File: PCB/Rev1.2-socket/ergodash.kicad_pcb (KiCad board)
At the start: 2 copper layers, 149.9 x 127.4 mm, 187 parts, among them J1 5PIN, J2 Conn_01x03, J3 Conn_01x03, J4 GS3, J5 GS3, M1 Speaker, Q1 IRLML6344TRPbF, SW1 SW_PUSH, SW10 SW_PUSH, SW11 SW_PUSH, SW12 SW_PUSH, SW13 SW_PUSH, SW14 SW_PUSH, SW15 SW_PUSH, SW16 SW_PUSH, SW17 SW_PUSH, SW18 SW_PUSH, SW19 SW_PUSH, SW2 SW_PUSH, SW20 SW_PUSH, SW21 SW_PUSH, SW22 SW_PUSH, SW23 SW_PUSH, SW24 SW_PUSH, SW25 SW_PUSH, SW26 SW_PUSH, SW27 SW_PUSH, SW28 SW_PUSH, SW29 SW_Push, SW3 SW_PUSH, SW30 SW_PUSH, SW31 SW_PUSH, SW32 SW_PUSH, SW33 SW_PUSH, SW34 SW_PUSH, SW35 SW_PUSH, SW36 SW_PUSH, SW37 SW_Push, SW38 SW_PUSH, SW39 SW_PUSH, SW4 SW_PUSH, SW40 SW_PUSH, SW41 SW_PUSH, SW5 SW_PUSH, SW6 SW_PUSH, SW7 SW_PUSH, SW8 SW_PUSH, SW9 SW_PUSH, U1 HOLE, U2 HOLE, U3 ProMicro, U4 HOLE, U5 HOLE, U6 ProMicro, U7 HOLE, U8 HOLE, U9 HOLE

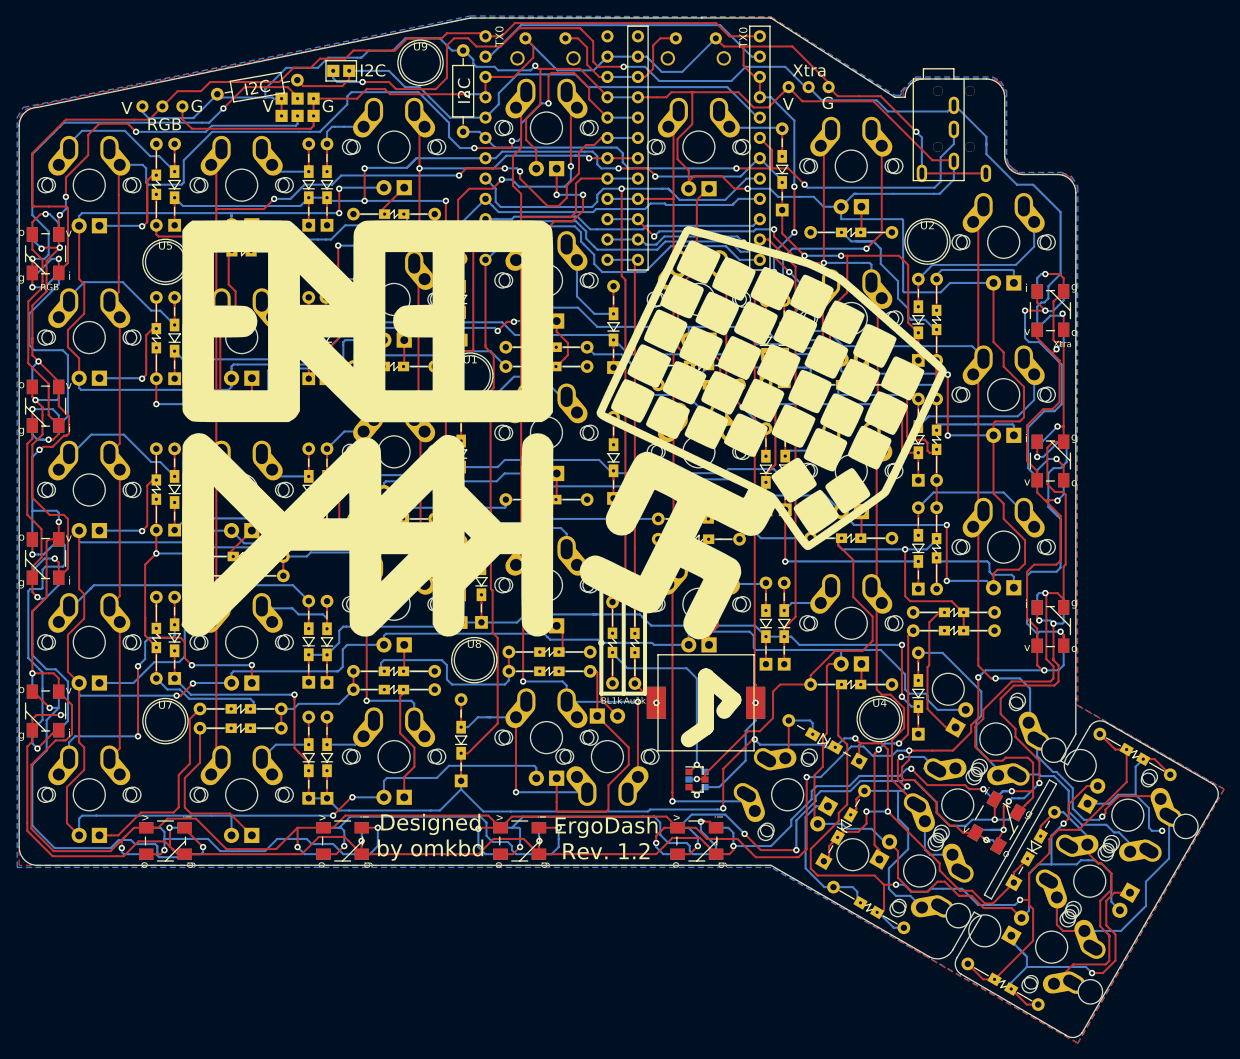
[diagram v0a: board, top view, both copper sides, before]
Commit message: Convert Rev1.2-socket project to KiCad 10 format
Open the legacy KiCad 5 project in KiCad 10 and save schematic and
board in the new format. Remove the legacy files (.pro/.sch/.net and
cache library) since symbols are now embedded in the .kicad_sch.
Ignore KiCad temporary files (.history/, lock files, backups).

Co-Authored-By: Claude Fable 5 <noreply@anthropic.com>
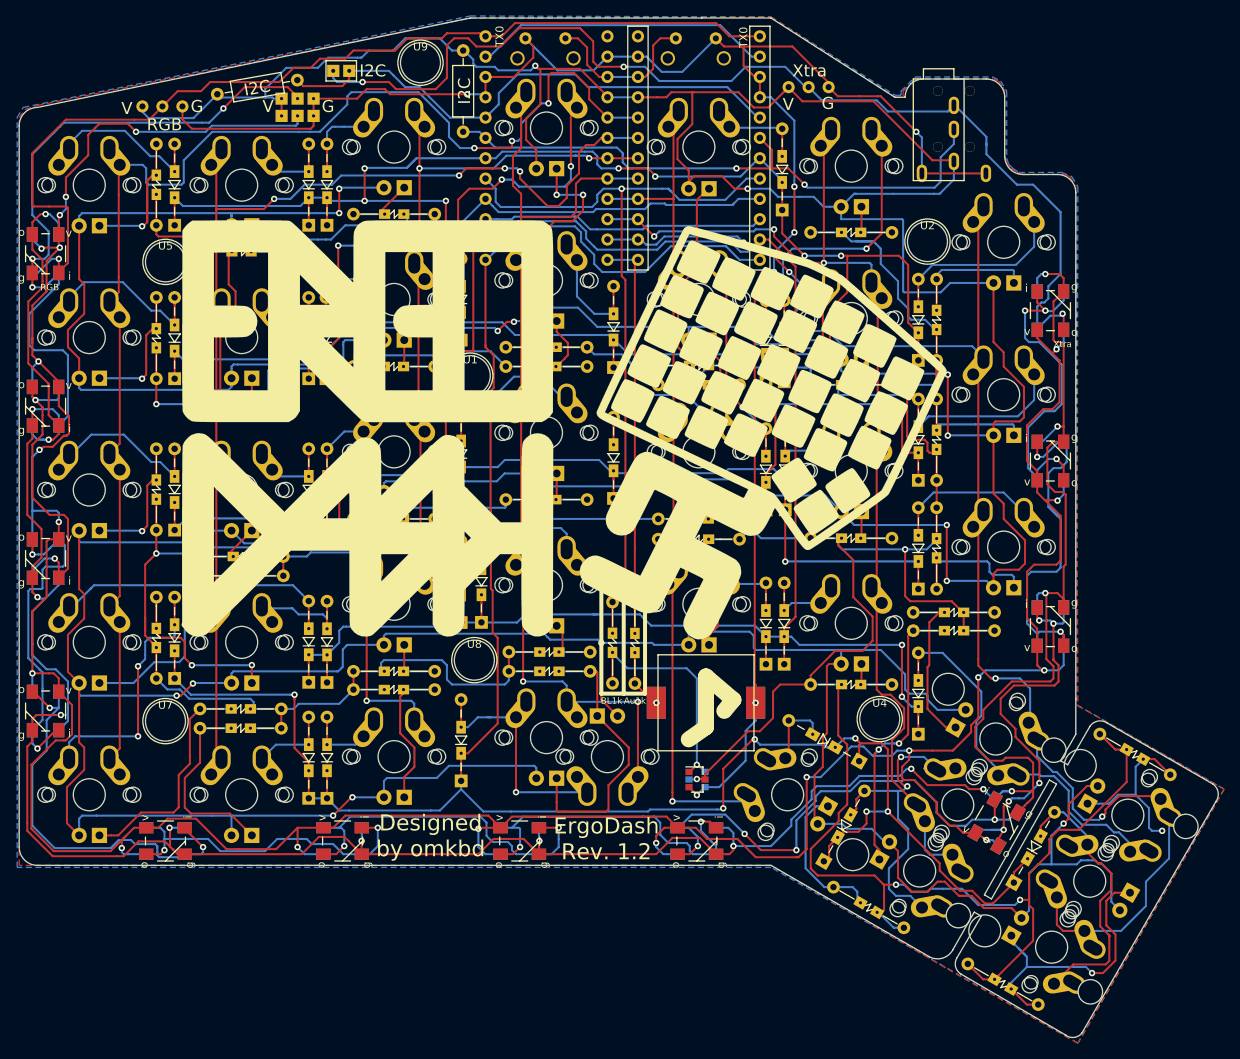
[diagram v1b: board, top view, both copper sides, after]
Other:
- net class Default removed

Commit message: Remove silkscreen logos and protect stabilizers from sync deletion
Drop the decorative logo footprints and mark the two 2U stabilizer
footprints as board-only so that updating the PCB from the schematic
with orphan deletion enabled will not remove them. Includes the
KiCad 10 resave of the board file.

Co-Authored-By: Claude Fable 5 <noreply@anthropic.com>
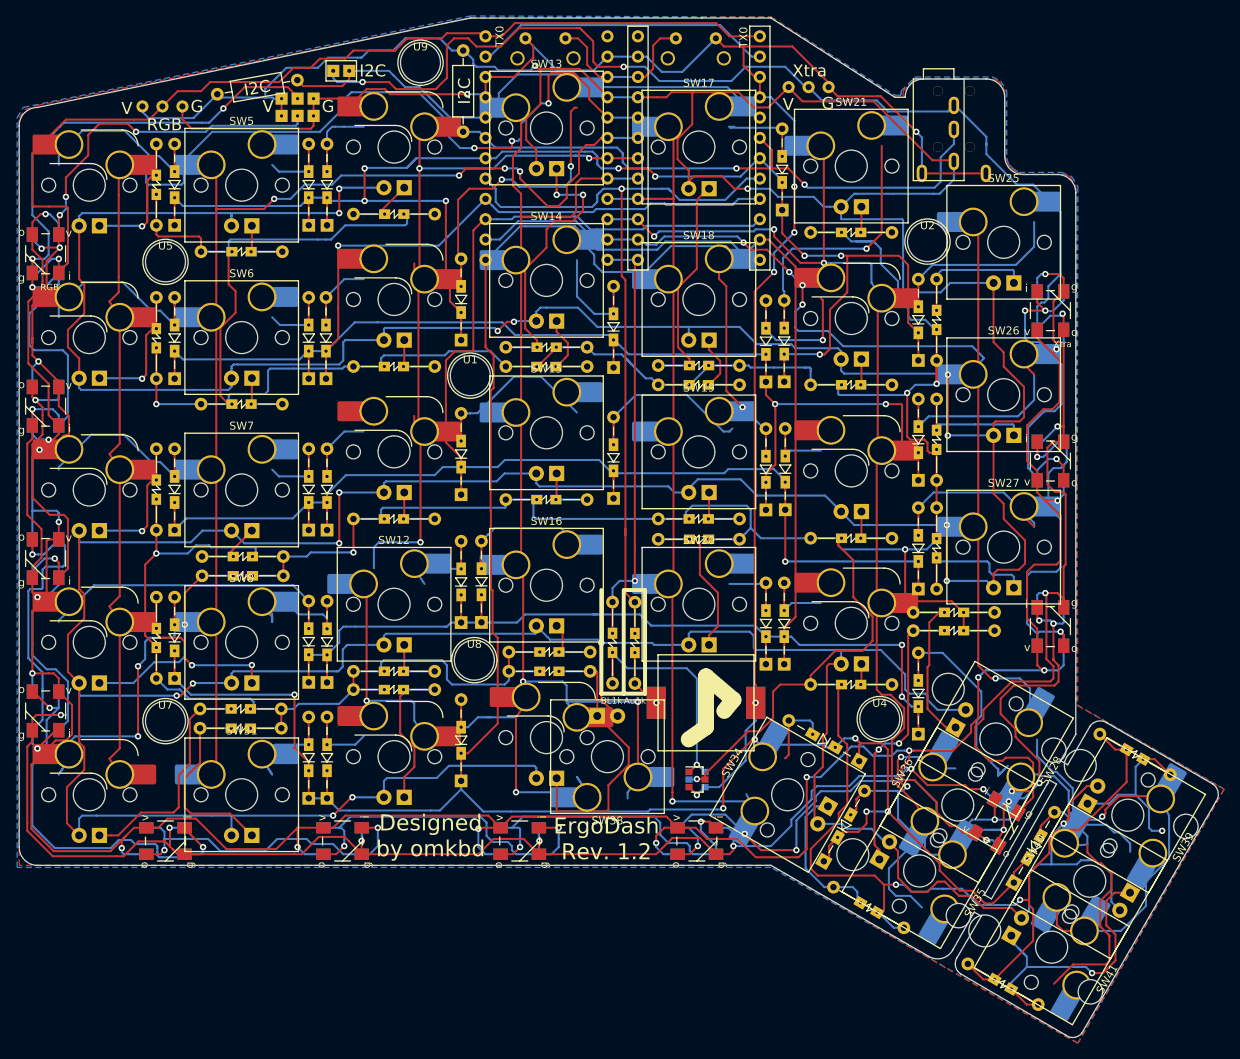
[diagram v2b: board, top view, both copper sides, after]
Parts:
- removed G***: LOGO, library:logo9
- removed G***: LOGO, library:logo8
- SW1, SW10, SW11, SW12, SW13, SW14, SW15, SW16, SW17, SW18, SW19, SW2, SW20, SW21, SW22, SW23, SW24, SW25, SW26, SW27, SW28, SW3, SW30, SW31, SW32, SW33, SW34, SW35, SW36, SW38, SW39, SW4, SW40, SW41, SW5, SW6, SW7, SW8, SW9: footprint library:MX_ALPS -> socket:SW_Hotswap_Kailh_MX_Plated
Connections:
- net /sda/uart renamed /sda/uart
- U3 pad 1: /RBG -> unconnected-(U3-TX-Pad1)
- U3 pad 13: /Backlight -> unconnected-(U3-B6-Pad13)
- U3 pad 24: (no net) -> unconnected-(U3-RAW-Pad24)
- U6 pad 1: /RBG -> unconnected-(U6-TX-Pad1)
- U6 pad 13: /Backlight -> unconnected-(U6-B6-Pad13)
- U6 pad 24: (no net) -> unconnected-(U6-RAW-Pad24)
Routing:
- net Net-(D34-Pad2): track 0.00 -> 43.7 mm, vias 0 -> 2
- net Net-(D34-A): track 43.7 -> 0.00 mm, vias 2 -> 0
- net Net-(D29-Pad2): track 0.00 -> 38.5 mm, vias 0 -> 2
- net Net-(D29-A): track 38.5 -> 0.00 mm, vias 2 -> 0
- net Net-(D68-Pad2): track 0.00 -> 37.9 mm
- net Net-(D68-A): track 37.9 -> 0.00 mm
- net Net-(D4-Pad2): track 0.00 -> 37.7 mm
- net Net-(D4-A): track 37.7 -> 0.00 mm
- net Net-(D13-Pad2): track 0.00 -> 36.4 mm, vias 0 -> 2
- net Net-(D13-A): track 36.4 -> 0.00 mm, vias 2 -> 0
- net Net-(D32-Pad2): track 0.00 -> 35.3 mm, vias 0 -> 1
- net Net-(D32-A): track 35.3 -> 0.00 mm, vias 1 -> 0
- net Net-(D18-Pad2): track 0.00 -> 26.7 mm, vias 0 -> 1
- net Net-(D18-A): track 26.7 -> 0.00 mm, vias 1 -> 0
- net Net-(D27-Pad2): track 0.00 -> 23.8 mm
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
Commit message: Sync board with socket schematic and clean up stale copper
Board-side result of the LED removal and switch footprint swap:
flip the 13 back-side socket footprints to the front (left-hand
board is no longer reversible), delete old tracks and vias that
shorted against or crowded the new socket pads, and refill the
copper zones. DRC violations drop from 1004 to 408; the remaining
ones are diode placement conflicts, rerouting work and alternative
layout courtyard overlaps to be resolved in the layout phase.

Co-Authored-By: Claude Fable 5 <noreply@anthropic.com>
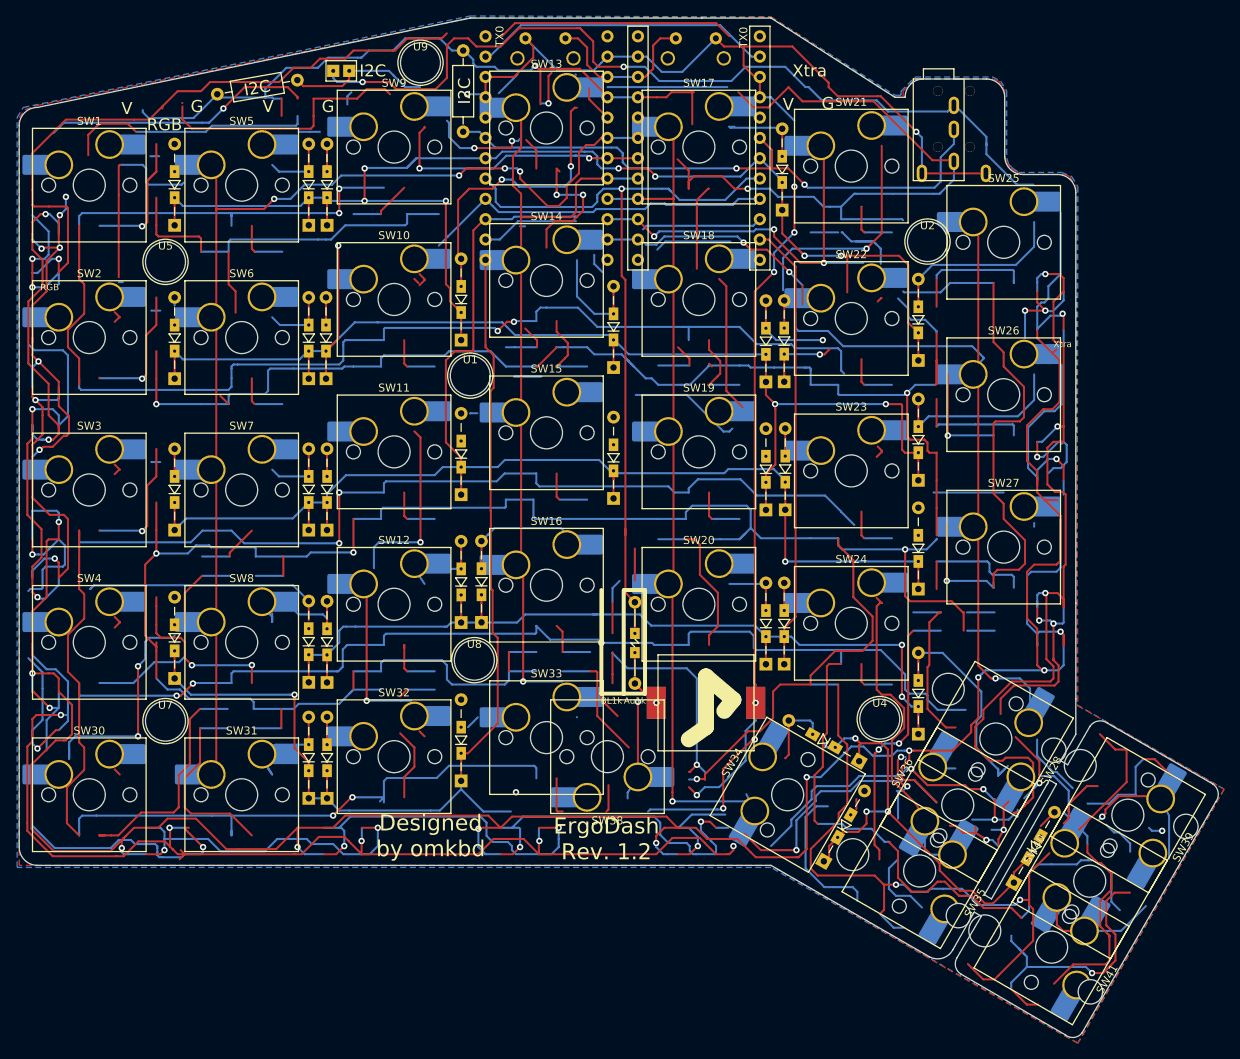
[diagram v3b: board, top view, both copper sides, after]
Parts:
- removed D35, D36, D37, D38, D39, D40, D41, D42, D43, D44, D45, D46, D47, D48, D49, D50, D51, D52, D53, D54, D55, D56, D57, D58, D59, D60, D61, D62, D63, D64, D65, D66, D67, D69, D70, D71, D72, D73: LED, library:CHERRY_MX_LED2
- removed J2, J3: Conn_01x03, library:conn3
- removed J4, J5: GS3, library:jumper2
- removed LED1, LED10, LED11, LED12, LED2, LED3, LED4, LED5, LED6, LED7, LED8, LED9: WS2812B, library:WS2812B-5
- removed Q1: IRLML6344TRPbF, library:SOT-23_2
- removed R10, R11, R12, R14, R15, R16, R17, R18, R19, R20, R21, R22, R23, R24, R25, R26, R27, R28, R29, R3, R30, R31, R32, R33, R34, R35, R36, R37, R38, R39, R4, R5, R6, R7, R8, R9: R, library:Resistors_SMD_THT
- removed R13: 1k, library:Resistors_SMD_THT
- SW1, SW10, SW11, SW2, SW22, SW23, SW24, SW3, SW30, SW32, SW33, SW4, SW9: moved to F.Cu
- turned SW1 to 0 degrees
- turned SW10 to 0 degrees
- turned SW11 to 0 degrees
- turned SW2 to 0 degrees
- turned SW22 to 0 degrees
- turned SW23 to 0 degrees
- turned SW24 to 0 degrees
- turned SW3 to 0 degrees
- turned SW30 to 0 degrees
- turned SW32 to 0 degrees
- turned SW33 to 0 degrees
- turned SW4 to 0 degrees
- turned SW9 to 0 degrees
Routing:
- net (no net): track 0.00 -> 2591.4 mm, vias 0 -> 81
- net Net-(Q1-Pad3): track 651.4 -> 0.00 mm, vias 9 -> 0
- net Net-(J4-Pad2): track 424.9 -> 0.00 mm, vias 16 -> 0
- net Net-(J5-Pad2): track 418.8 -> 0.00 mm, vias 20 -> 0
- net /RBG: track 124.4 -> 0.00 mm, vias 1 -> 0
- net Net-(D28-A): track 29.0 -> 133.8 mm, vias 0 -> 3
- net VCC: track 953.4 -> 856.0 mm, vias 18 -> 15
- net /col0: track 175.2 -> 101.9 mm
- net Net-(LED8-Pad4): track 65.9 -> 0.00 mm, vias 4 -> 0
- net /row4: track 281.4 -> 215.5 mm
- net /Backlight: track 52.9 -> 0.00 mm, vias 1 -> 0
- net Net-(LED10-Pad2): track 51.7 -> 0.00 mm, vias 5 -> 0
- net Net-(LED4-Pad4): track 51.6 -> 0.00 mm, vias 2 -> 0
- net Net-(LED10-Pad4): track 46.5 -> 0.00 mm, vias 2 -> 0
- net Net-(LED6-Pad4): track 44.2 -> 0.00 mm, vias 2 -> 0
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
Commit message: Resolve socket collisions around the Pro Micro
The hotswap socket pads of the four keys above the controllers
shorted against Pro Micro pin pads. Fix in three parts: exclude U6
(the right-hand controller, unused on the left board) from the
board via on_board=no, rotate SW13/SW14 by 270 degrees so their
socket wings thread the corridor between the U3 pin columns
(min copper gap 0.27mm), and remove the stale tracks under the
rotated pads. Netlist diff confirms the only schematic change is
U6 dropping out of the PCB netlist.

Also includes manual diode repositioning done in the GUI.

Co-Authored-By: Claude Fable 5 <noreply@anthropic.com>
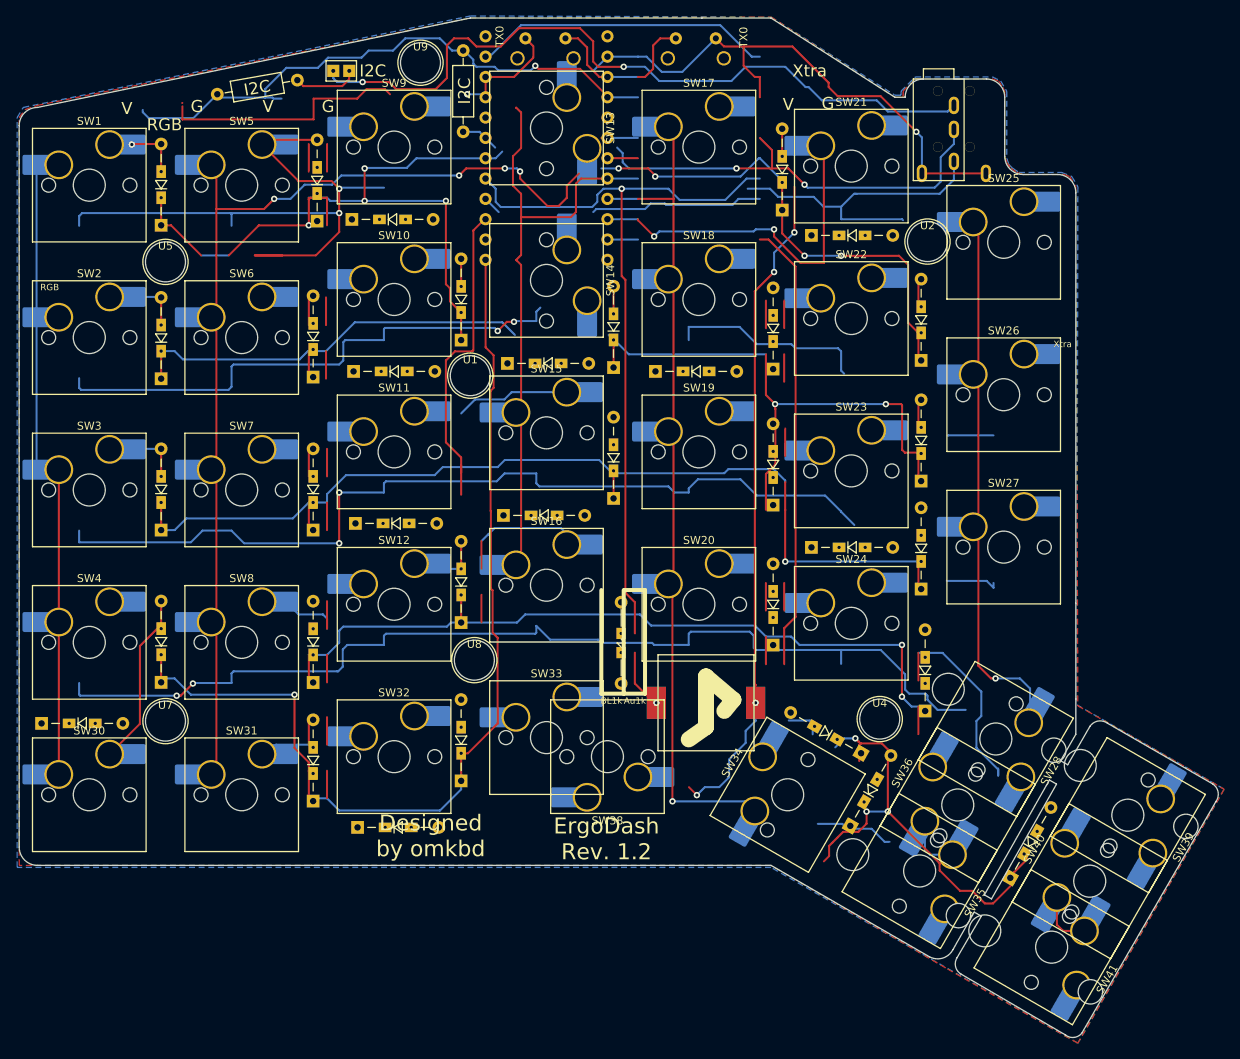
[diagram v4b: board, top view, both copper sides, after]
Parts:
- removed U6: ProMicro, library:ProMicro_rev
- moved D18 22.1 mm to (157.8, 81.3), turned to 0 degrees
- moved D21 18.6 mm to (177.3, 64.3), turned to 0 degrees
- moved D4 18.4 mm to (96.0, 120.1)
- moved D29 17.6 mm to (81.0, 125.3), turned to 0 degrees
- moved D15 17.4 mm to (139.3, 80.3), turned to 0 degrees
- moved D24 15.0 mm to (177.3, 103.3), turned to 0 degrees
- moved D16 13.7 mm to (138.8, 99.3), turned to 0 degrees
- moved D34 5.53 mm to (182.1, 138.1)
- moved D31 5.27 mm to (120.5, 138.3), turned to 0 degrees
- moved D11 3.65 mm to (120.3, 100.3), turned to 0 degrees
- moved D10 3.56 mm to (120.0, 81.3), turned to 0 degrees
- moved D9 3.19 mm to (119.8, 62.3), turned to 0 degrees
- moved D28 3.01 mm to (191.5, 123.7)
- moved D20 2.55 mm to (172.5, 115.5)
- moved D22 1.84 mm to (172.5, 81.0)
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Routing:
- net (no net): track 2591.4 -> 0.00 mm, vias 81 -> 0
- net VCC: track 856.0 -> 126.1 mm, vias 15 -> 1
- net Net-(D18-A): track 0.00 -> 112.7 mm, vias 0 -> 2
- net Net-(D28-A): track 133.8 -> 26.1 mm, vias 3 -> 0
- net /row3: track 189.6 -> 294.3 mm, vias 2 -> 4
- net /col6: track 169.9 -> 79.8 mm, vias 4 -> 1
- net /col2: track 81.4 -> 3.81 mm, vias 4 -> 0
- net Net-(D5-A): track 8.37 -> 80.9 mm, vias 0 -> 2
- net /row1: track 198.4 -> 246.0 mm, vias 3 -> 4
- net /col5: track 93.9 -> 52.7 mm, vias 3 -> 2
- net /xtradata: track 130.7 -> 92.8 mm, vias 3 -> 2
- net /col3: track 112.0 -> 78.3 mm, vias 2 -> 0
- net Net-(D13-A): track 36.4 -> 3.45 mm, vias 2 -> 0
- net Net-(D4-A): track 30.9 -> 0.00 mm
- net Net-(D21-A): track 32.0 -> 3.45 mm, vias 1 -> 0
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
